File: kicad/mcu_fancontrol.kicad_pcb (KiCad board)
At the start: 2 copper layers, 60 x 32 mm, 51 parts, among them J1 Vin, J10 Output2, J11 NTC2, J2 I2C, J3 I2C, J4 1-Wire, J5 1-Wire, J6 SWIM, J7 UART, J8 NTC1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

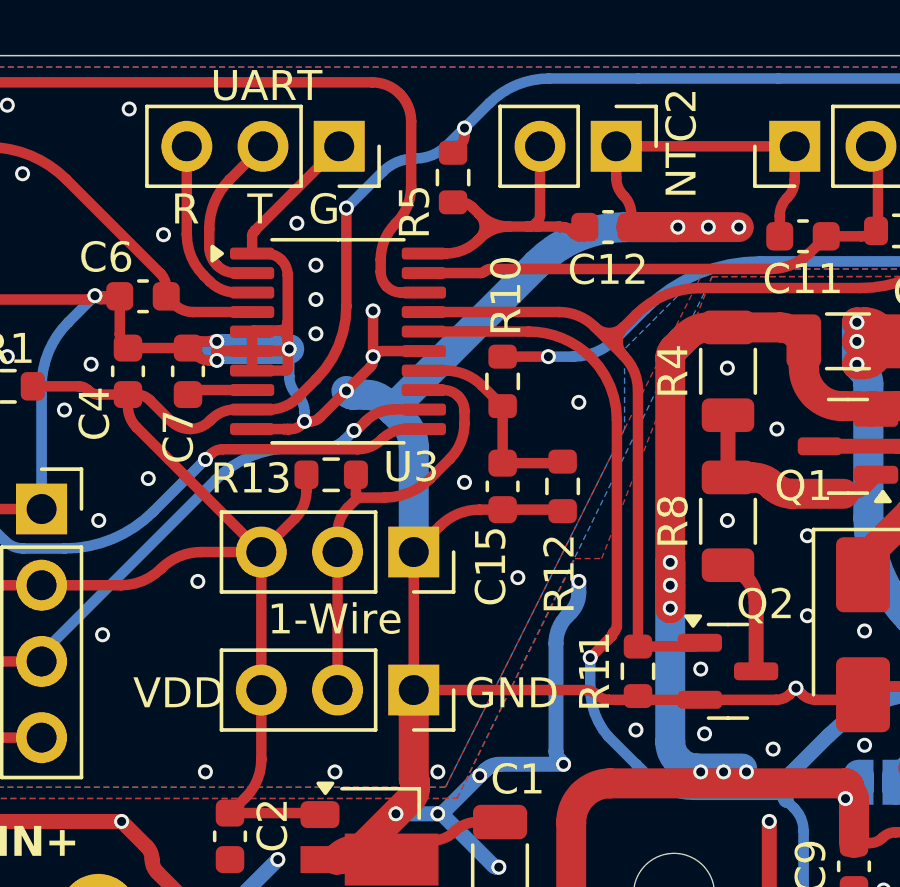
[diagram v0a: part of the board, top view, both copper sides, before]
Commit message: pcb: Fix ground plane
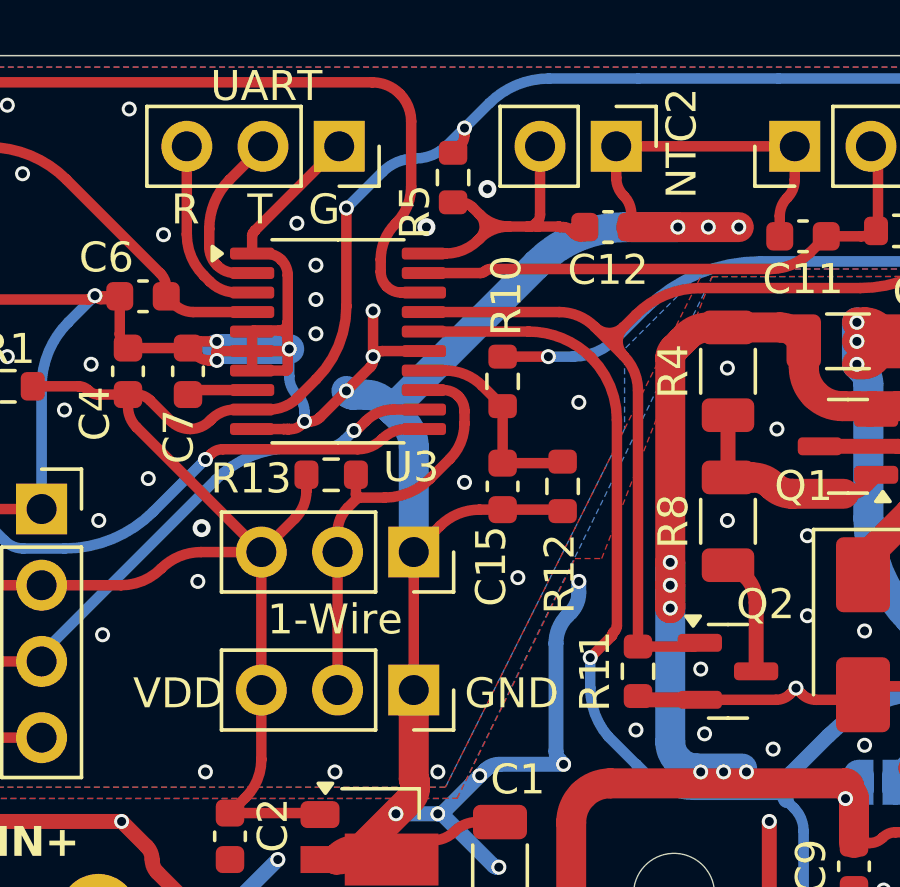
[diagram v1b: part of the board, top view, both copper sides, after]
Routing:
- net GND: track 313.1 -> 305.6 mm, vias 113 -> 116

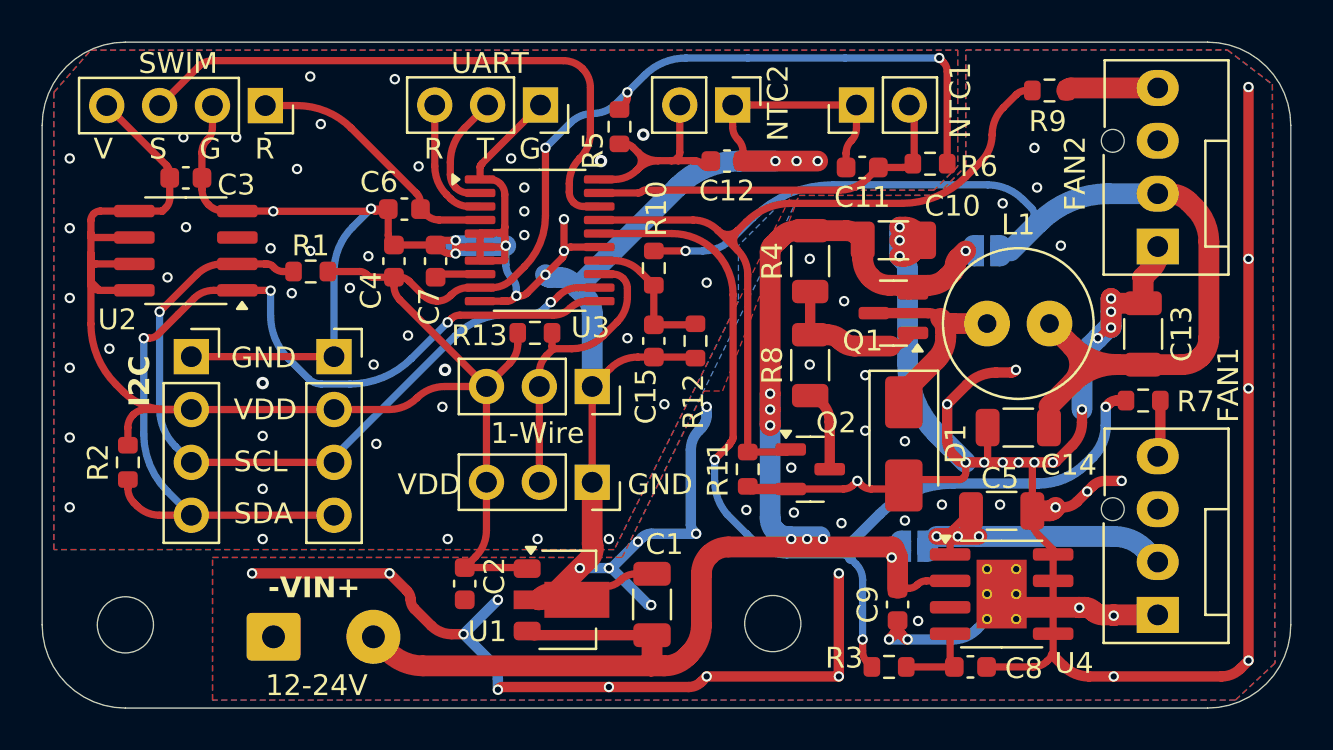
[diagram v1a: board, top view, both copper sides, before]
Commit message: pcb: Minor change in the ground plane
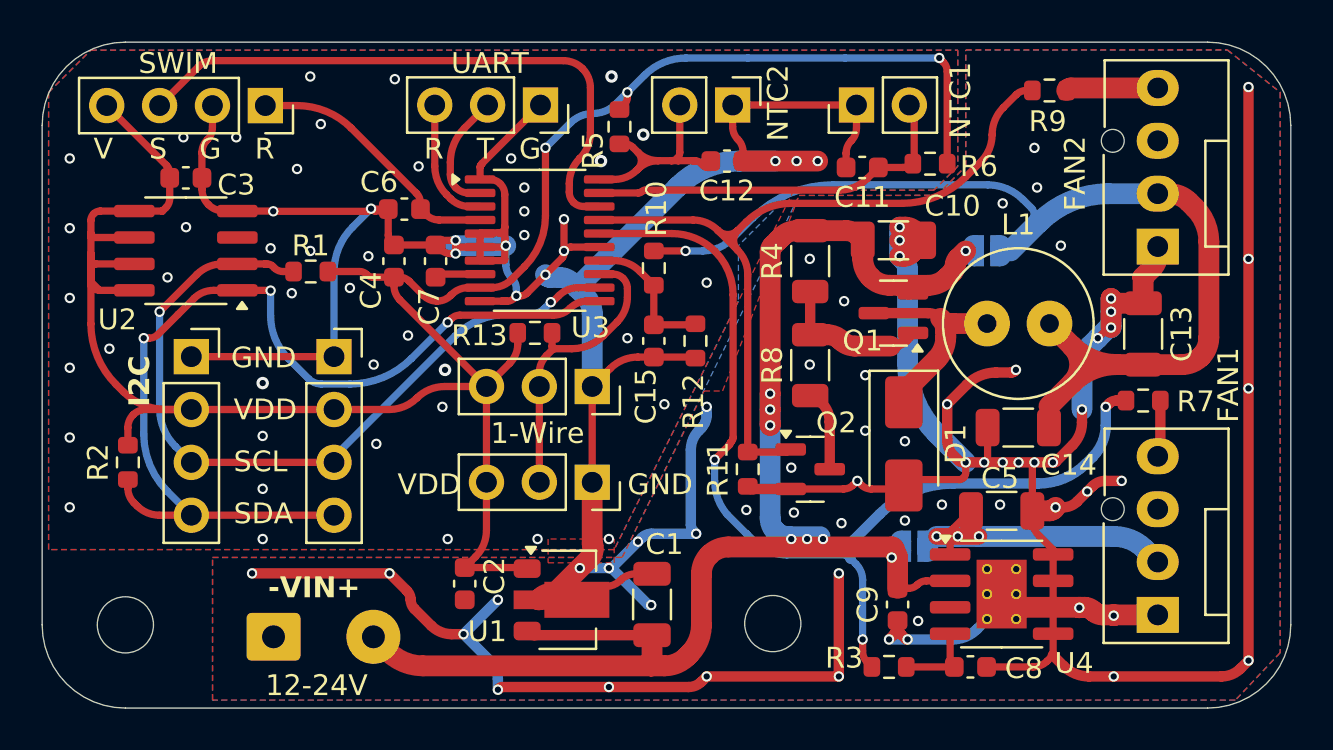
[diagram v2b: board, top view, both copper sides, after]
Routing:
- net GND: vias 116 -> 117

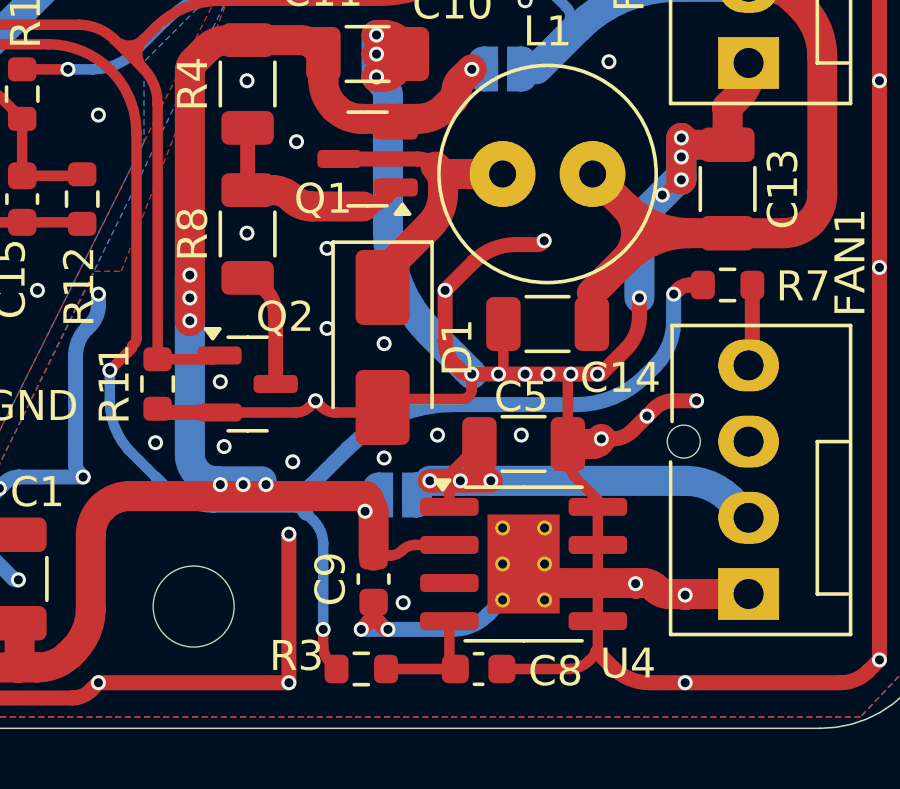
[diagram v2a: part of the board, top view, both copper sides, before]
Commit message: pcb: Fix ground plane
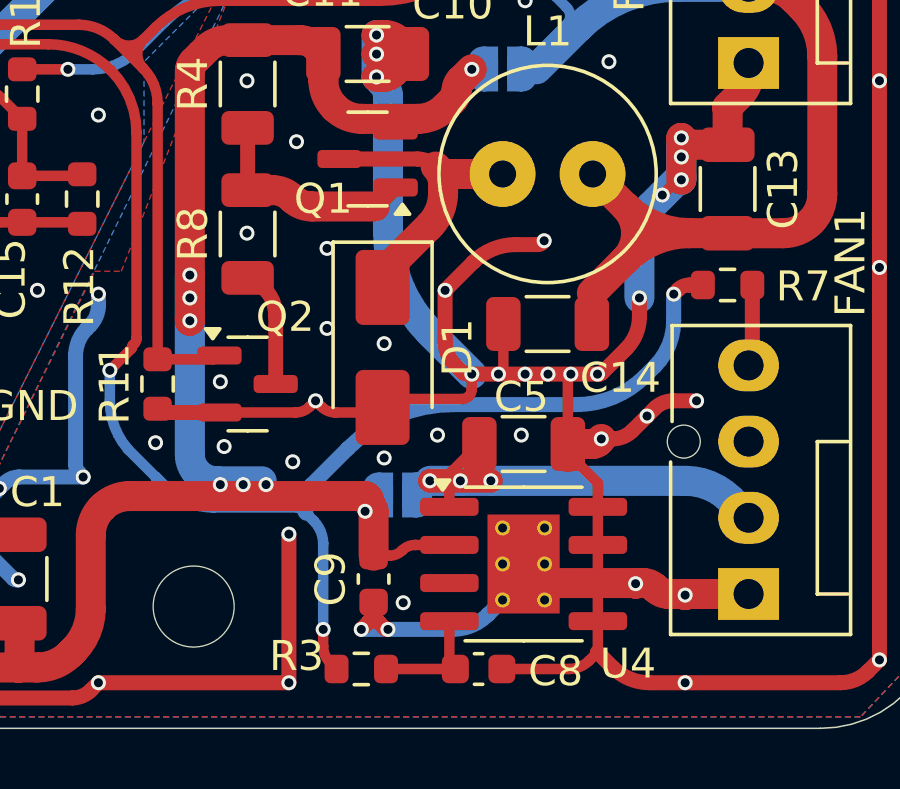
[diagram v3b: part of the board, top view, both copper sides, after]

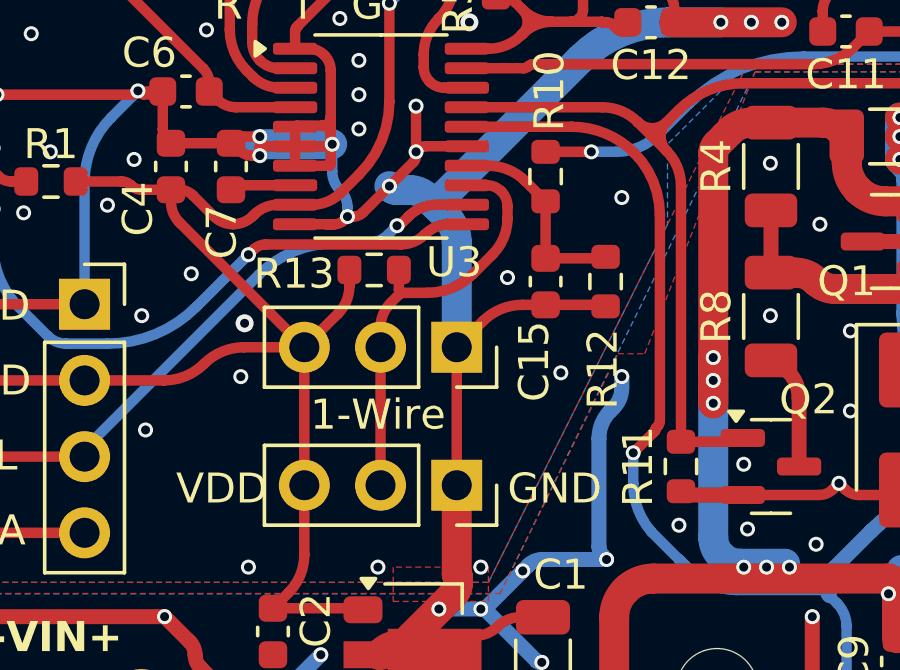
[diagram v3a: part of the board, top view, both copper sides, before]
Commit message: pcb: Add optional RC filter for 1-Wire
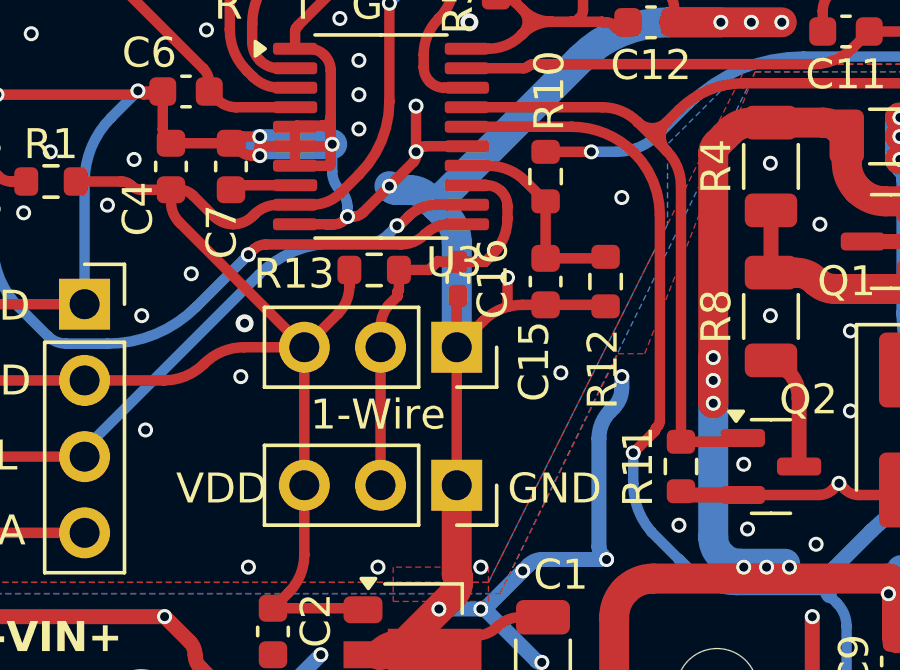
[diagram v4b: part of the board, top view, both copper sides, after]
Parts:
- added C16: 180pF, Capacitor_SMD:C_0402_1005Metric_Pad0.74x0.62mm_HandSolder, F.Cu at (147.1, 92.2)
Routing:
- net GND: track 305.7 -> 308.4 mm
